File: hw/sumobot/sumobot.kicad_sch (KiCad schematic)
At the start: 30 parts

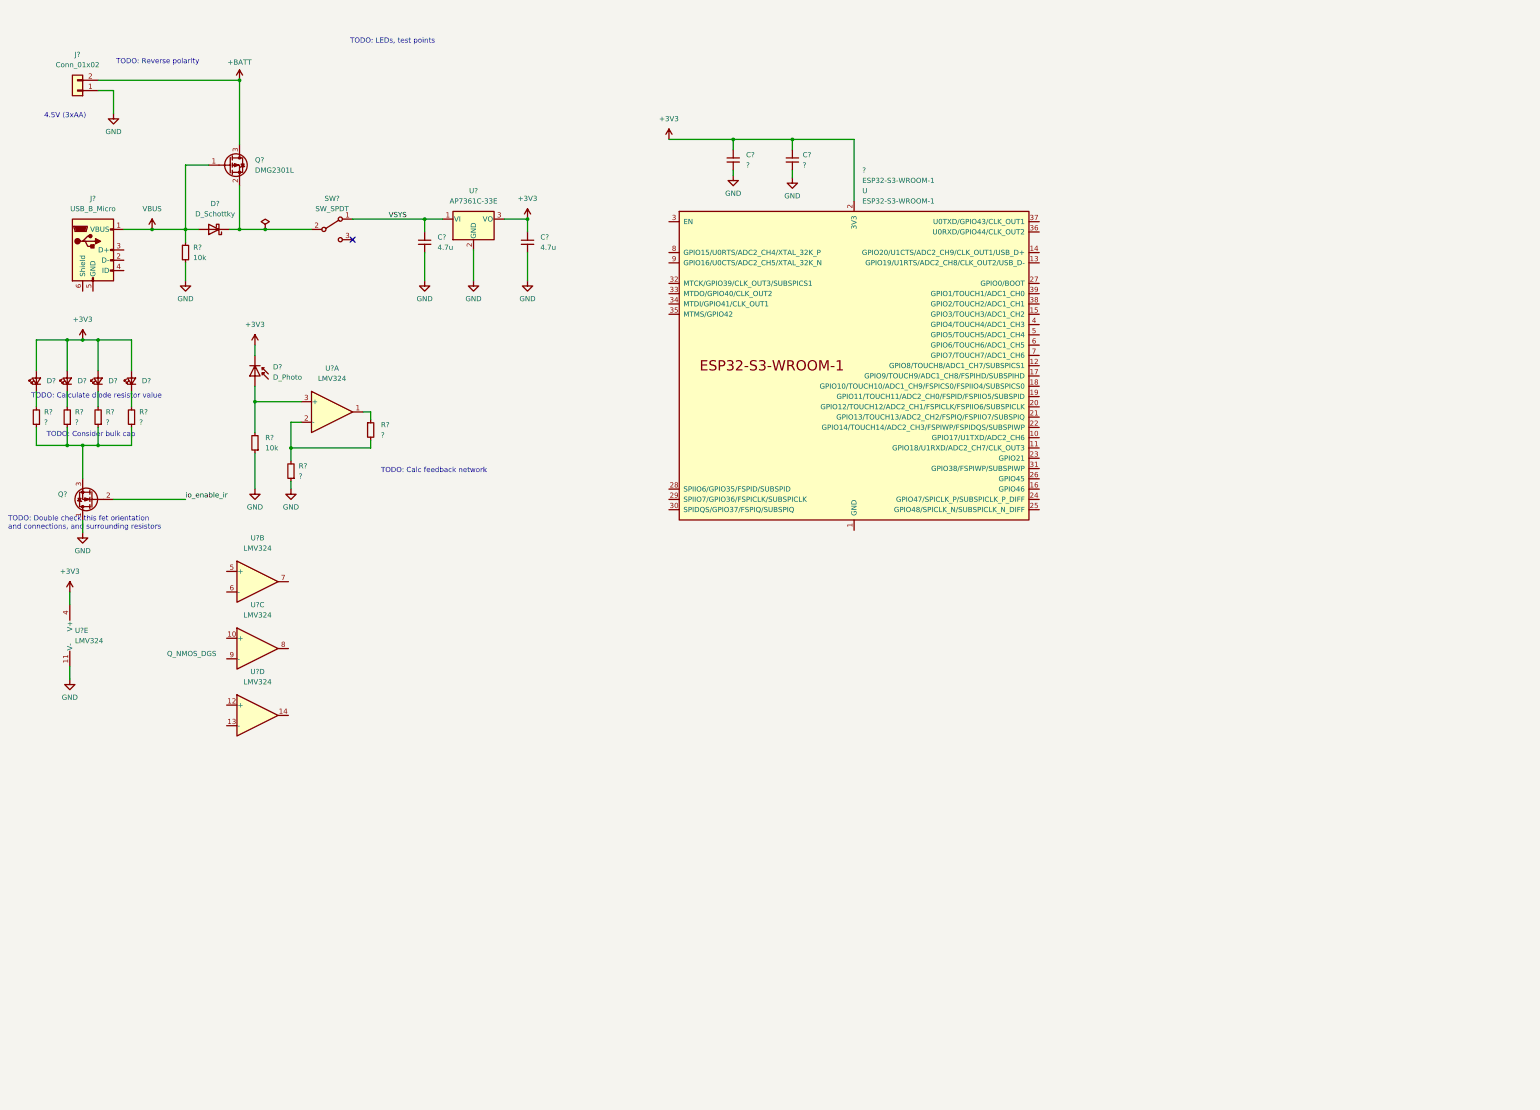
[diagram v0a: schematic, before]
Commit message: Schematic before cleanup and footprints
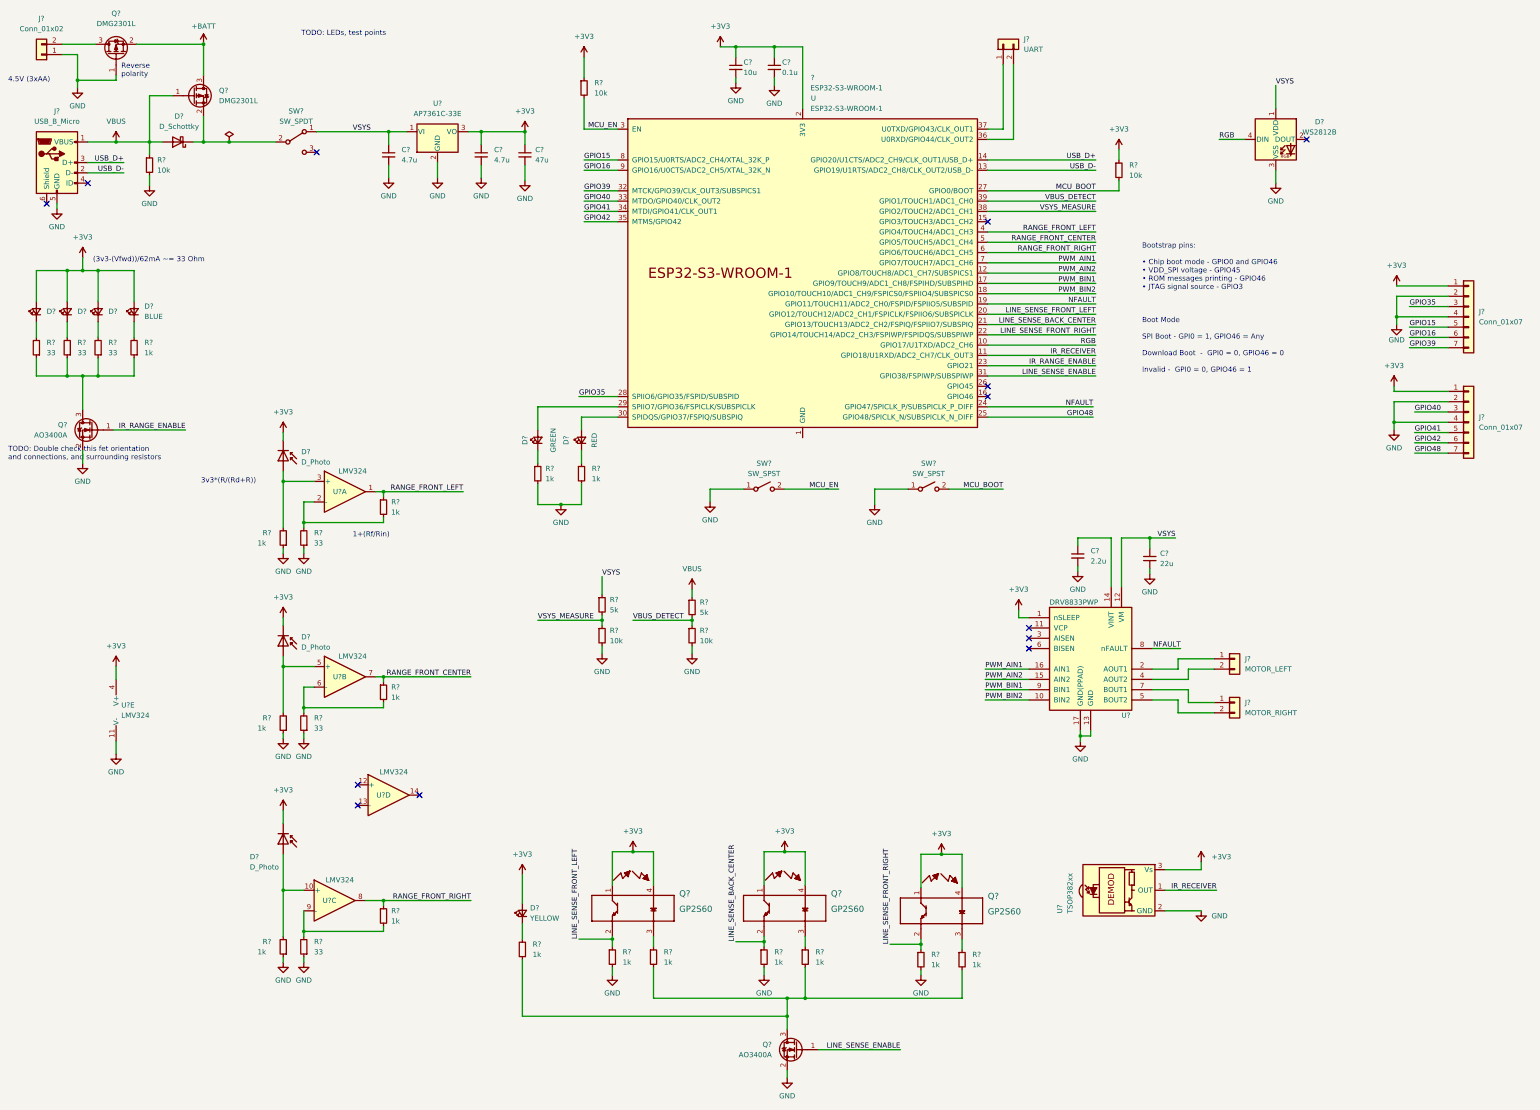
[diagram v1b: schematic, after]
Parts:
- removed D?: LED_Small, symbol Device:LED_Small
- removed Q?: Q_NMOS_DGS, symbol Device:Q_NMOS_DGS
- removed R?: ?, symbol Device:R_Small
- added C?: 47u, symbol Device:C_Small
- added C?: 2.2u, symbol Device:C_Small
- added C?: 22u, symbol Device:C_Small
- added D? (x2): D_Photo, symbol Device:D_Photo
- added D?: BLUE, symbol Device:LED_Small
- added D?: WS2812B, LED_SMD:LED_WS2812B_PLCC4_5.0x5.0mm_P3.2mm, symbol LED:WS2812B
- added D?: GREEN, symbol Device:LED_Small
- added D?: RED, symbol Device:LED_Small
- added D?: YELLOW, symbol Device:LED_Small
- added J?: MOTOR_LEFT, symbol Connector_Generic:Conn_01x02
- added J?: MOTOR_RIGHT, symbol Connector_Generic:Conn_01x02
- added J?: UART, symbol Connector_Generic:Conn_01x02
- added J? (x2): Conn_01x07, symbol Connector_Generic:Conn_01x07
- added Q? (x2): AO3400A, Package_TO_SOT_SMD:SOT-23, symbol Transistor_FET:AO3400A
- added Q? (x3): GP2S60, TRAN_ICA00550_SHP, symbol QRsumo_symbols:GP2S60
- added Q?: DMG2301L, Package_TO_SOT_SMD:SOT-23, symbol Transistor_FET:DMG2301L
- added R? (x14): 1k, symbol Device:R_Small
- added R? (x4): 10k, symbol Device:R_Small
- added R? (x2): 33, symbol Device:R_Small
- added R? (x2): 5k, symbol Device:R_Small
- added SW? (x2): SW_SPST, symbol Switch:SW_SPST
- added U?: TSOP382xx, OptoDevice:Vishay_MINICAST-3Pin, symbol Interface_Optical:TSOP382xx
- added U?: DRV8833PWP, Package_SO:HTSSOP-16-1EP_4.4x5mm_P0.65mm_EP3.4x5mm_Mask2.46x2.31mm_ThermalVias, symbol Driver_Motor:DRV8833PWP
- C?: value ? -> 10u
- C?: value ? -> 0.1u
- R?: value ? -> 1k
- R? (x4): value ? -> 33
- R?: value 10k -> 1k
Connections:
- net +3V3: now also C?.1, D?.1 (K), D?.1 (K), D?.2 (A), D?.2 (A), J?.1 (Pin_1), J?.1 (Pin_1), Q?.1, Q?.1, Q?.1, Q?.4, Q?.4, Q?.4, R?.1, R?.1, U?.1 (nSLEEP), U?.3 (Vs)
- net +BATT: now also Q?.2 (S); no longer J?.2 (Pin_2)
- net GND: now also J?.5 (GND), C?.2, C?.2, C?.2, D?.3 (VSS), J?.2 (Pin_2), J?.2 (Pin_2), J?.4 (Pin_4), J?.4 (Pin_4), Q?.1 (G), Q?.2 (S), Q?.2 (S), R?.1, R?.1, R?.1, R?.1, R?.2, R?.2, R?.2, R?.2, R?.2, R?.2, R?.2, SW?.1 (A), SW?.1 (A), U?.13 (GND), U?.17 (GND(PPAD)), U?.2 (GND)
- net VBUS: now also R?.1
- net VSYS: now also C?.1, D?.1 (VDD), R?.1, U?.12 (VM)
- net USB_D-: now reaches J?.2 (D-)
- net USB_D-: now also ?.13 (GPIO19/U1RTS/ADC2_CH8/CLK_OUT2/USB_D-)
- net USB_D+: now reaches J?.3 (D+)
- net USB_D+: now also ?.14 (GPIO20/U1CTS/ADC2_CH9/CLK_OUT1/USB_D+)
- net RANGE_FRONT_LEFT: now reaches R?.1, U?.1
- net RANGE_FRONT_LEFT: now also ?.4 (GPIO4/TOUCH4/ADC1_CH3)
- net at R?.1, R?.1, R?.1: now also Q?.3 (D), R?.1
- net at U?.10 (+): now also D?.2 (A), R?.2
- net RANGE_FRONT_RIGHT: now reaches U?.8
- net RANGE_FRONT_RIGHT: now also ?.6 (GPIO6/TOUCH6/ADC1_CH5), R?.1
- net at U?.9 (-): now also R?.2, R?.2
- net at U?.5 (+): now also D?.2 (A), R?.2
- net at U?.6 (-): now also R?.2, R?.2
- net RANGE_FRONT_CENTER: now reaches U?.7
- net RANGE_FRONT_CENTER: now also ?.5 (GPIO5/TOUCH5/ADC1_CH4), R?.1
- net RGB: now reaches ?.10 (GPIO17/U1TXD/ADC2_CH6)
- net RGB: now also D?.4 (DIN)
- net IR_RECEIVER: now reaches ?.11 (GPIO18/U1RXD/ADC2_CH7/CLK_OUT3)
- net IR_RECEIVER: now also U?.1 (OUT)
- net PWM_AIN2: now reaches ?.12 (GPIO8/TOUCH8/ADC1_CH7/SUBSPICS1)
- net PWM_AIN2: now also U?.15 (AIN2)
- net PWM_BIN1: now reaches ?.17 (GPIO9/TOUCH9/ADC1_CH8/FSPIHD/SUBSPIHD)
- net PWM_BIN1: now also U?.9 (BIN1)
- net PWM_BIN2: now reaches ?.18 (GPIO10/TOUCH10/ADC1_CH9/FSPICS0/FSPIIO4/SUBSPICS0)
- net PWM_BIN2: now also U?.10 (BIN2)
- net NFAULT: now reaches ?.19 (GPIO11/TOUCH11/ADC2_CH0/FSPID/FSPIIO5/SUBSPID)
- net NFAULT: now also ?.24 (GPIO47/SPICLK_P/SUBSPICLK_P_DIFF), U?.8 (nFAULT)
- net LINE_SENSE_FRONT_LEFT: now reaches ?.20 (GPIO12/TOUCH12/ADC2_CH1/FSPICLK/FSPIIO6/SUBSPICLK)
- net LINE_SENSE_FRONT_LEFT: now also Q?.2, R?.1
- net LINE_SENSE_BACK_CENTER: now reaches ?.21 (GPIO13/TOUCH13/ADC2_CH2/FSPIQ/FSPIIO7/SUBSPIQ)
- net LINE_SENSE_BACK_CENTER: now also Q?.2, R?.1
- net LINE_SENSE_FRONT_RIGHT: now reaches ?.22 (GPIO14/TOUCH14/ADC2_CH3/FSPIWP/FSPIDQS/SUBSPIWP)
- net LINE_SENSE_FRONT_RIGHT: now also Q?.2, R?.1
- net IR_RANGE_ENABLE: now reaches ?.23 (GPIO21)
- net IR_RANGE_ENABLE: now also Q?.1 (G)
- net GPIO48: now reaches ?.25 (GPIO48/SPICLK_N/SUBSPICLK_N_DIFF)
- net GPIO48: now also J?.7 (Pin_7)
- net MCU_BOOT: now reaches ?.27 (GPIO0/BOOT)
- net MCU_BOOT: now also R?.2, SW?.2 (B)
- net GPIO35: now reaches ?.28 (SPIIO6/GPIO35/FSPID/SUBSPID)
- net GPIO35: now also J?.3 (Pin_3)
- net at ?.29 (SPIIO7/GPIO36/FSPICLK/SUBSPICLK): now also D?.2 (A)
- net MCU_EN: now reaches ?.3 (EN)
- net MCU_EN: now also R?.2, SW?.2 (B)
- net at ?.30 (SPIDQS/GPIO37/FSPIQ/SUBSPIQ): now also D?.2 (A)
- net LINE_SENSE_ENABLE: now reaches ?.31 (GPIO38/FSPIWP/SUBSPIWP)
- net LINE_SENSE_ENABLE: now also Q?.1 (G)
- net GPIO39: now reaches ?.32 (MTCK/GPIO39/CLK_OUT3/SUBSPICS1)
- net GPIO39: now also J?.7 (Pin_7)
- net GPIO40: now reaches ?.33 (MTDO/GPIO40/CLK_OUT2)
- net GPIO40: now also J?.3 (Pin_3)
- net GPIO41: now reaches ?.34 (MTDI/GPIO41/CLK_OUT1)
- net GPIO41: now also J?.5 (Pin_5)
- net GPIO42: now reaches ?.35 (MTMS/GPIO42)
- net GPIO42: now also J?.6 (Pin_6)
- net at ?.36 (U0RXD/GPIO44/CLK_OUT2): now also J?.2 (Pin_2)
- net at ?.37 (U0TXD/GPIO43/CLK_OUT1): now also J?.1 (Pin_1)
- net VSYS_MEASURE: now reaches ?.38 (GPIO2/TOUCH2/ADC1_CH1)
- net VSYS_MEASURE: now also R?.1, R?.2
- net VBUS_DETECT: now reaches ?.39 (GPIO1/TOUCH1/ADC1_CH0)
- net VBUS_DETECT: now also R?.1, R?.2
- net PWM_AIN1: now reaches ?.7 (GPIO7/TOUCH7/ADC1_CH6)
- net PWM_AIN1: now also U?.16 (AIN1)
- net GPIO15: now reaches ?.8 (GPIO15/U0RTS/ADC2_CH4/XTAL_32K_P)
- net GPIO15: now also J?.5 (Pin_5)
- net GPIO16: now reaches ?.9 (GPIO16/U0CTS/ADC2_CH5/XTAL_32K_N)
- net GPIO16: now also J?.6 (Pin_6)
- new net: J?.1 (Pin_1), U?.2 (AOUT1)
- new net: J?.2 (Pin_2), U?.4 (AOUT2)
- new net: J?.1 (Pin_1), U?.7 (BOUT1)
- new net: J?.2 (Pin_2), U?.5 (BOUT2)
- new net: D?.1 (K), R?.2 (x2)
- new net: Q?.3 (D), R?.1, R?.2, R?.2, R?.2
- new net: Q?.3, R?.1 (x3)
- new net: D?.1 (K), R?.1 (x2)
- new net: C?.1, U?.14 (VINT)
- new net: J?.2 (Pin_2), Q?.3 (D)
- no-connect marks 1 -> 13
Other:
- note added: "(3v3-(Vfwd))/62mA ~= 33 Ohm"
- note added: "1+(Rf/Rin)"
- note added: "3v3*(R/(Rd+R))"
- note added: "Bootstrap pins: • Chip boot mode - GPIO0 and GPIO46 • VDD_SPI voltage - GPIO45 • ROM messages printing - GPIO46 • JTAG signal source - GPIO3 Boot Mode SPI Boot - GPI0 = 1, GPIO46 = Any Download Boot - GPI0 = 0, GPIO46 = 0 Invalid - GPI0 = 0, GPIO46 = 1"
- note added: "Reverse polarity"
- note removed: "TODO: Calc feedback network"
- note removed: "TODO: Calculate diode resistor value"
- note removed: "TODO: Consider bulk cap"
- note removed: "TODO: Reverse polarity"
- moved on the sheet: ?, C?, D?, J?, Q?, R?, SW?, U?, U?A, U?B, U?C, U?D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

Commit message: Schematic finished
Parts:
- removed J?: UART, symbol Connector_Generic:Conn_01x02
- added C8: 10u, Capacitor_SMD:C_0603_1608Metric, symbol Device:C_Small
- added J3: UART, Connector_PinHeader_2.54mm:PinHeader_1x03_P2.54mm_Vertical, symbol Connector_Generic:Conn_01x03
- added J8: VBAT, Connector_PinHeader_2.54mm:PinHeader_1x02_P2.54mm_Vertical, symbol Connector_Generic:Conn_01x02
- added R30, R32: 10k, Resistor_SMD:R_0603_1608Metric, symbol Device:R_Small
- added R31, R33: 100, Resistor_SMD:R_0603_1608Metric, symbol Device:R_Small
- C1, C2, C3, C4, C5, C6, C7: renamed from C?; footprint (none) -> Capacitor_SMD:C_0603_1608Metric
- D1, D2, D3, D6, D7, D8: renamed from D?; footprint (none) -> Connector_PinHeader_2.54mm:PinHeader_1x02_P2.54mm_Vertical
- D10, D11, D4, D9: renamed from D?; footprint (none) -> LED_SMD:LED_0603_1608Metric
- D5: renamed from D?; footprint (none) -> Diode_SMD:D_SOD-123F
- J1, J4, J5: renamed from J?; footprint (none) -> Connector_PinHeader_2.54mm:PinHeader_1x02_P2.54mm_Vertical
- J2: renamed from J?; footprint (none) -> QRsumo_FootprintLibrary:CONN_10118193-0001LF_AMP
- J6, J7: renamed from J?; footprint (none) -> Connector_PinHeader_2.54mm:PinHeader_1x07_P2.54mm_Vertical
- Q4, Q5, Q7: renamed from Q?; footprint TRAN_ICA00550_SHP -> QRsumo_FootprintLibrary:SHARP_GP2S60
- R1, R10, R11, R12, R13, R14, R15, R16, R17, R18, R19, R2, R20, R21, R22, R23, R24, R25, R26, R27, R28, R29, R3, R4, R5, R6, R7, R8, R9: renamed from R?; footprint (none) -> Resistor_SMD:R_0603_1608Metric
- SW2, SW3: renamed from SW?; footprint (none) -> QRsumo_FootprintLibrary:PTS647_SPST_SNXX_SMTR2_4.5x4.5mm
- U1: renamed from U?; footprint (none) -> Package_SO:TSSOP-14_4.4x5mm_P0.65mm
- U5: renamed from ?; footprint (none) -> Espressif:ESP32-S3-WROOM-1U
- gave numbers to parts that had none: 9
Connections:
- net +BATT: now also J8.1 (Pin_1)
- net GND: now also U5.1 (GND), U5.40 (GND), U5.41 (GND), C8.2, J3.3 (Pin_3), J8.2 (Pin_2), R30.1, R32.1
- net IR_RANGE_ENABLE: now also R31.1; no longer Q1.1 (G)
- net LINE_SENSE_ENABLE: now also R33.1; no longer Q6.1 (G)
- net NFAULT: no longer U5.24 (GPIO47/SPICLK_P/SUBSPICLK_P_DIFF)
- net VSYS: now also C8.1
- net AOUT1: now reaches J4.1 (Pin_1), U3.2 (AOUT1)
- net AOUT2: now reaches J4.2 (Pin_2), U3.4 (AOUT2)
- net BOUT1: now reaches J5.1 (Pin_1), U3.7 (BOUT1)
- net BOUT2: now reaches J5.2 (Pin_2), U3.5 (BOUT2)
- net LINE_SENSE: now reaches Q6.3 (D), R15.1, R22.2, R26.2, R28.2
- net UART_TX0: now reaches U5.37 (U0TXD/GPIO43/CLK_OUT1)
- net UART_TX0: now also J3.1 (Pin_1)
- net UART_RX0: now reaches U5.36 (U0RXD/GPIO44/CLK_OUT2)
- net UART_RX0: now also J3.2 (Pin_2)
- net BAT_UNPROT: now reaches J1.2 (Pin_2), Q2.3 (D)
- new net: Q6.1 (G), R32.2, R33.2
- new net: Q1.1 (G), R30.2, R31.2
- no-connect marks 13 -> 14
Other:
- note added: "TODO: Measure power consumption when switch off."
- note removed: "TODO: Double check this fet orientation and connections, and surrounding resistors"
- note removed: "TODO: LEDs, test points"
- moved on the sheet: C1, C2, C3, D1, D12, D2, D3, D4, D5, D6, D7, D8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
